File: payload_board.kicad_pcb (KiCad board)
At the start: 4 copper layers, 100 x 100 mm, 100 parts, among them IC1 RP2040_QFN56, IC2 AZ1117CH-3.3TRG1, J1 Cam_PicoLock, J10 503398-1892, J12 FC Breakout, J15 SWC, J2 Cam_Conn, J3 Antenna_Conn, J4 usb jumper, J5 Display_Conn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

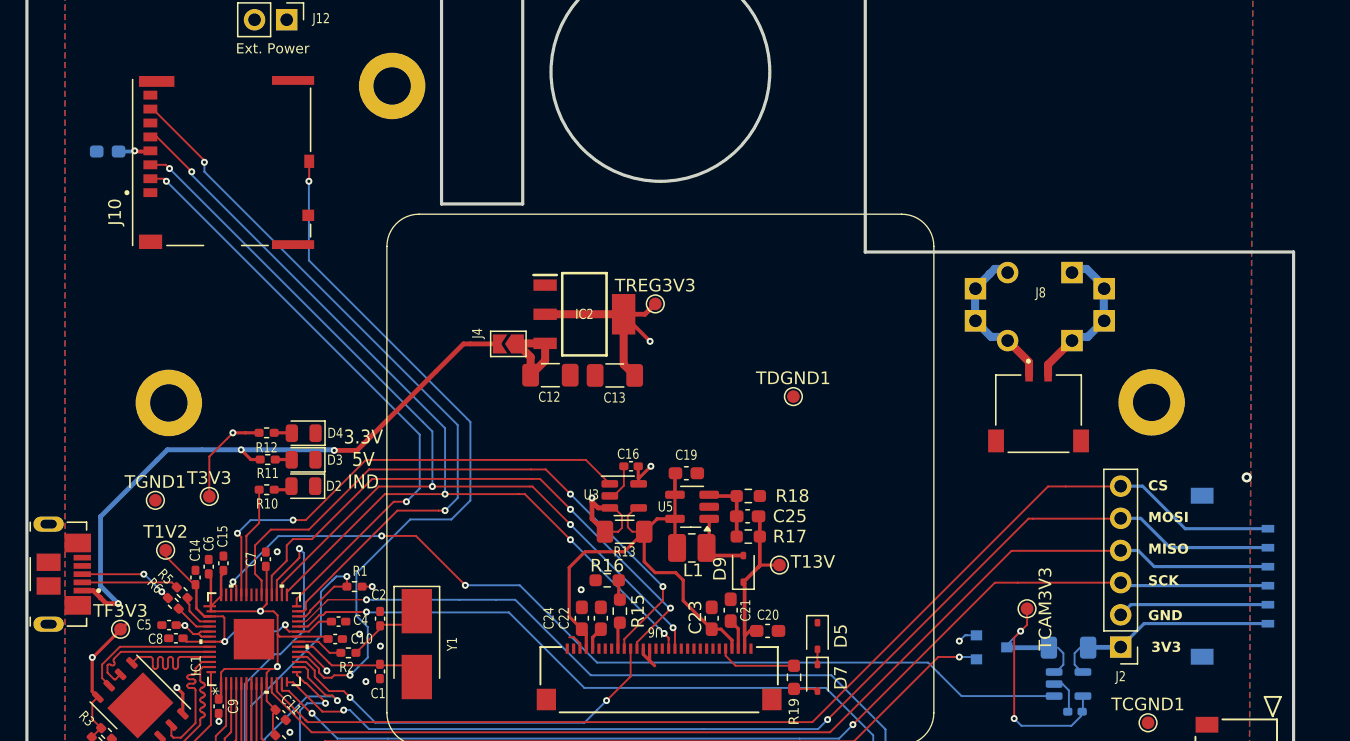
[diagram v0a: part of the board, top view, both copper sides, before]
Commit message: Moved the final connector from back to front, footprint kepout for chasis mounts and moved sd card
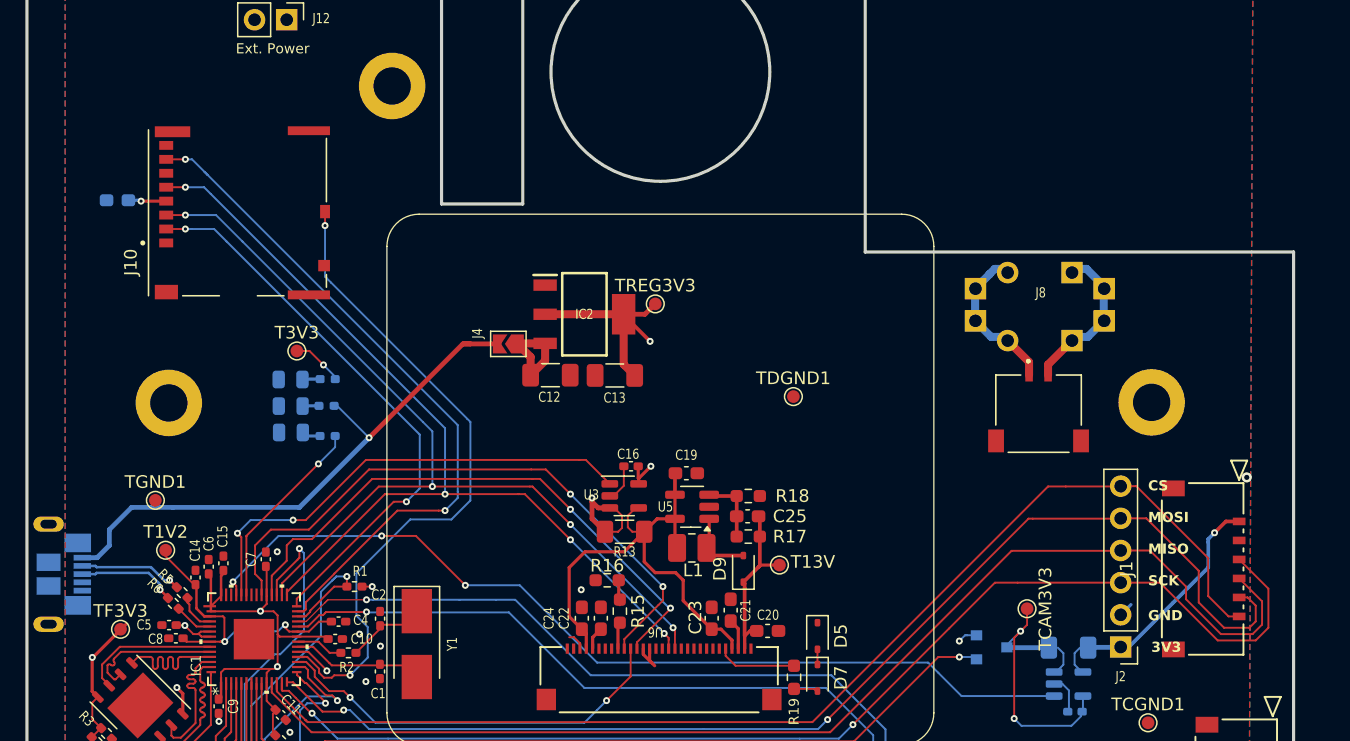
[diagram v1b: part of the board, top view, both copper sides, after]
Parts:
- D2, D3, D4, J7, R10, R11, R12: moved to B.Cu
- J1: moved to F.Cu
- moved T3V3 13.4 mm to (34.3, 58.9)
- moved J1 8.39 mm to (108.7, 72.4), turned to 90 degrees
- moved R12 6.42 mm to (36.7, 61.1), turned to 0 degrees
- moved R10 6.41 mm to (36.7, 65.6), turned to 0 degrees
- moved R11 6.29 mm to (36.6, 63.2), turned to 0 degrees
- moved D4 4.36 mm to (33.8, 61.1), turned to 0 degrees
- moved D3 4.36 mm to (33.8, 63.2), turned to 0 degrees
- moved D2 4.35 mm to (33.8, 65.3), turned to 0 degrees
- moved J10 4.16 mm to (29.6, 48.0)
- moved C18 3.92 mm to (20.1, 47.0)
- turned J7 to 90 degrees
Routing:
- net GND: track 27.9 -> 16.8 mm
- net SPI1_SCK_Cam: track 85.4 -> 94.1 mm
- net SPI1_MISO_Cam: track 87.4 -> 94.2 mm
- net Net-(IC1-GPIO25): track 8.81 -> 15.5 mm, vias 0 -> 1
- net SPI1_MOSI_Cam: track 87.1 -> 93.0 mm
- net VBUS: track 49.8 -> 45.0 mm, vias 3 -> 1
- net SD_IND: track 57.6 -> 53.1 mm
- net +3.3V: track 95.8 -> 92.3 mm
- net SPI0_MISO: track 57.6 -> 54.5 mm
- net SPI0_SCK: track 77.2 -> 74.2 mm
- net SPI0_CS_SD: track 47.8 -> 44.9 mm
- net SPI0_MOSI: track 77.1 -> 74.2 mm
- net SPI1_CS_Cam: track 89.2 -> 91.5 mm
- net CIN-: track 17.3 -> 19.4 mm, vias 0 -> 1
- net /D-: track 7.90 -> 8.16 mm, vias 0 -> 1
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
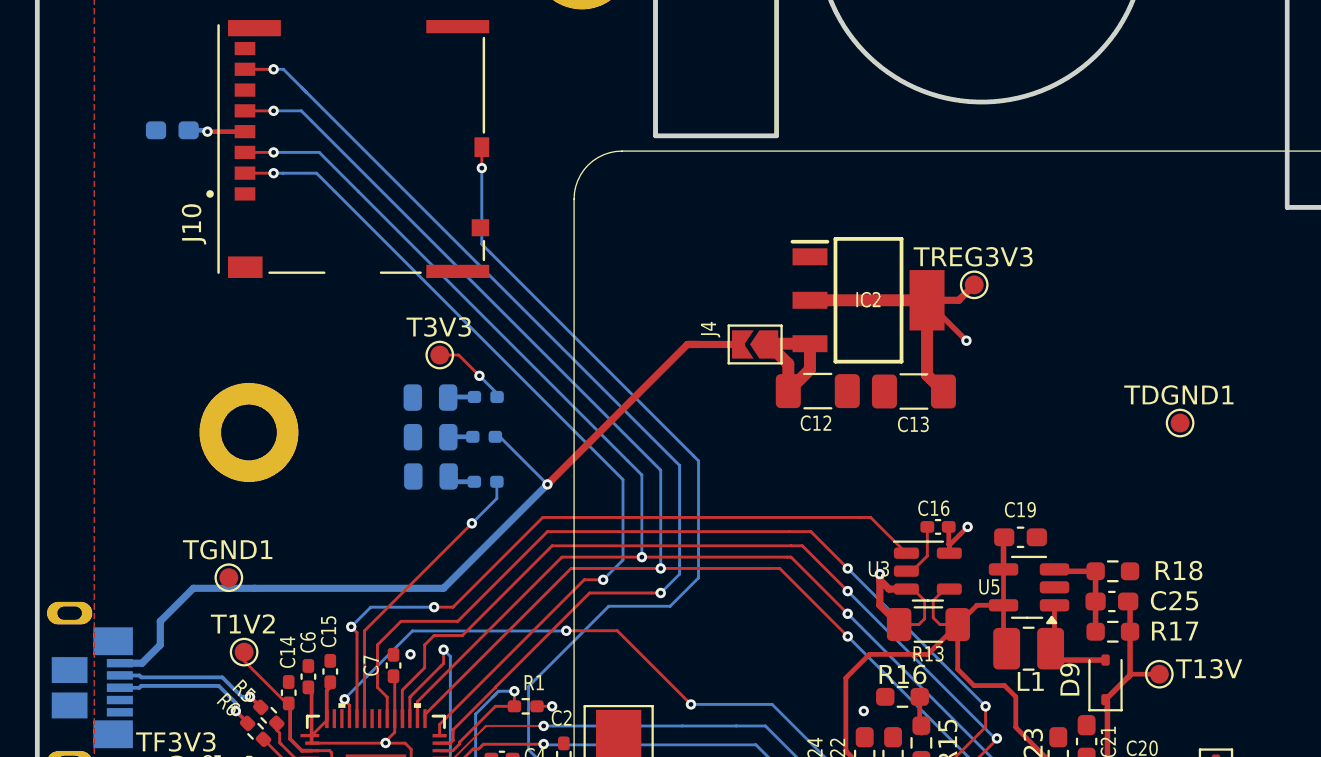
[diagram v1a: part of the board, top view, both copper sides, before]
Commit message: Changed some components to decrease bom count (C18, C25)
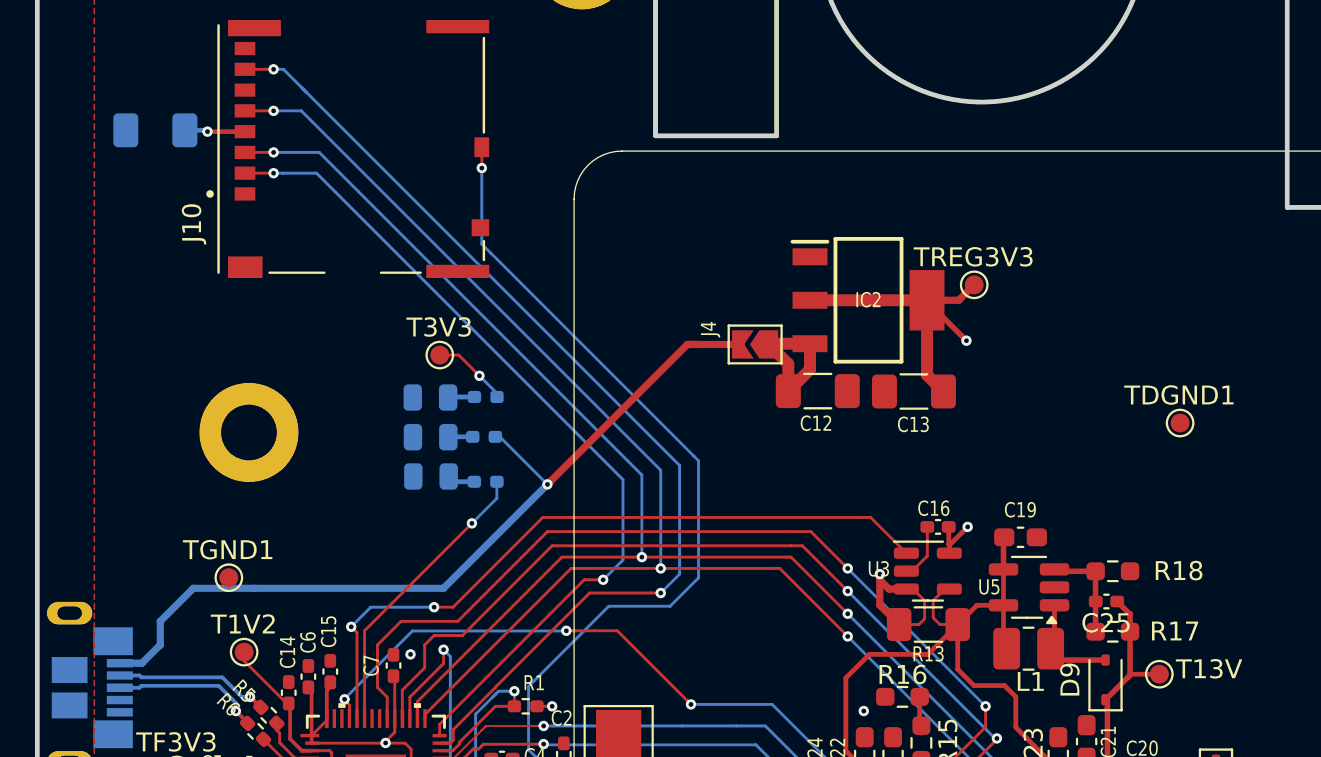
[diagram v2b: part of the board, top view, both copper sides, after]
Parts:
- C18: footprint Capacitor_SMD:C_0603_1608Metric_Pad1.08x0.95mm_HandSolder -> Capacitor_SMD:C_1206_3216Metric_Pad1.33x1.80mm_HandSolder
- C25: footprint Capacitor_SMD:C_0603_1608Metric_Pad1.08x0.95mm_HandSolder -> Capacitor_SMD:C_0402_1005Metric_Pad0.74x0.62mm_HandSolder
- moved C18 0.90 mm to (19.2, 47.0)
- moved C25 0.29 mm to (69.6, 72.0)
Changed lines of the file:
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@@
 		)
 	)
-	(footprint "Capacitor_SMD:C_0603_1608Metric_Pad1.08x0.95mm_HandSolder"
+	(footprint "Capacitor_SMD:C_0402_1005Metric_Pad0.74x0.62mm_HandSolder"
 		(layer "F.Cu")
-		(at 69.887499 71.95 180)
-		(descr "Capacitor SMD 0603 (1608 Metric), square (rectangular) end terminal, IPC_7351 nominal with elongated pad for handsoldering. (Body size source: IPC-SM-782 page 76, https://www.pcb-3d.com/wordpress/wp-content/uploads/ipc-sm-782a_amendment_1_and_2.pdf), generated with kicad-footprint-generator")
+		(at 69.6 71.95 180)
+		(descr "Capacitor SMD 0402 (1005 Metric), square (rectangular) end terminal, IPC_7351 nominal with elongated pad for handsoldering. (Body size source: IPC-SM-782 page 76, https://www.pcb-3d.com/wordpress/wp-content/uploads/ipc-sm-782a_amendment_1_and_2.pdf), generated with kicad-footprint-generator")
 		(tags "capacitor handsolder")
 		(property "Reference" "C25"
-			(at -3.3375 0 0)
+			(at 0 -1.16 180)
 			(layer "F.SilkS")
 			(effects
@@
 		)
 		(property "Value" "0.1uF"
-			(at 0 1.43 0)
+			(at 0 1.16 180)
 			(layer "F.Fab")
 			(effects
@@
 			)
 		)
-		(property "Footprint" "Capacitor_SMD:C_0603_1608Metric_Pad1.08x0.95mm_HandSolder"
+		(property "Footprint" "Capacitor_SMD:C_0402_1005Metric_Pad0.74x0.62mm_HandSolder"
 			(at 0 0 180)
 			(unlocked yes)
@@
 		(attr smd)
 		(fp_line
-			(start -0.146267 0.51)
-			(end 0.146267 0.51)
+			(start -0.115835 0.36)
+			(end 0.115835 0.36)
 			(stroke
 				(width 0.12)
@@
 		)
 		(fp_line
-			(start -0.146267 -0.51)
-			(end 0.146267 -0.51)
+			(start -0.115835 -0.36)
+			(end 0.115835 -0.36)
 			(stroke
 				(width 0.12)
@@
 		)
 		(fp_line
-			(start 1.65 0.73)
-			(end -1.65 0.73)
+			(start 1.08 0.46)
+			(end -1.08 0.46)
 			(stroke
 				(width 0.05)
@@
 		)
 		(fp_line
-			(start 1.65 -0.73)
-			(end 1.65 0.73)
+			(start 1.08 -0.46)
+			(end 1.08 0.46)
 			(stroke
 				(width 0.05)
@@
 		)
 		(fp_line
-			(start -1.65 0.73)
-			(end -1.65 -0.73)
+			(start -1.08 0.46)
+			(end -1.08 -0.46)
 			(stroke
 				(width 0.05)
@@
 		)
 		(fp_line
-			(start -1.65 -0.73)
-			(end 1.65 -0.73)
+			(start -1.08 -0.46)
+			(end 1.08 -0.46)
 			(stroke
 				(width 0.05)
@@
 		)
 		(fp_line
-			(start 0.8 0.4)
-			(end -0.8 0.4)
+			(start 0.5 0.25)
+			(end -0.5 0.25)
 			(stroke
 				(width 0.1)
@@
 		)
 		(fp_line
-			(start 0.8 -0.4)
-			(end 0.8 0.4)
+			(start 0.5 -0.25)
+			(end 0.5 0.25)
 			(stroke
 				(width 0.1)
@@
 		)
 		(fp_line
-			(start -0.8 0.4)
-			(end -0.8 -0.4)
+			(start -0.5 0.25)
+			(end -0.5 -0.25)
 			(stroke
 				(width 0.1)
@@
 		)
 		(fp_line
-			(start -0.8 -0.4)
-			(end 0.8 -0.4)
+			(start -0.5 -0.25)
+			(end 0.5 -0.25)
 			(stroke
 				(width 0.1)
@@
 		)
 		(fp_text user "${REFERENCE}"
-			(at 0 0 0)
+			(at 0 0 180)
 			(layer "F.Fab")
 			(effects
 				(font
-					(size 0.4 0.4)
-					(thickness 0.06)
+					(size 0.25 0.25)
+					(thickness 0.04)
 				)
 			)
 		)
 		(pad "1" smd roundrect
-			(at -0.8625 0 180)
-			(size 1.075 0.95)
+			(at -0.5675 0 180)
+			(size 0.735 0.62)
 			(layers "F.Cu" "F.Paste" "F.Mask")
 			(roundrect_rratio 0.25)
@@
 		)
 		(pad "2" smd roundrect
-			(at 0.8625 0 180)
-			(size 1.075 0.95)
+			(at 0.5675 0 180)
+			(size 0.735 0.62)
 			(layers "F.Cu" "F.Paste" "F.Mask")
 			(roundrect_rratio 0.25)
@@
 			(pintype "passive")
 		)
-		(model "${KICAD8_3DMODEL_DIR}/Capacitor_SMD.3dshapes/C_0603_1608Metric.wrl"
+		(model "${KICAD8_3DMODEL_DIR}/Capacitor_SMD.3dshapes/C_0402_1005Metric.wrl"
 			(offset
 				(xyz 0 0 0)
@@
 		)
 	)
-	(footprint "Capacitor_SMD:C_0603_1608Metric_Pad1.08x0.95mm_HandSolder"
+	(footprint "Capacitor_SMD:C_1206_3216Metric_Pad1.33x1.80mm_HandSolder"
 		(layer "B.Cu")
-		(at 20.1375 47)
-		(descr "Capacitor SMD 0603 (1608 Metric), square (rectangular) end terminal, IPC_7351 nominal with elongated pad for handsoldering. (Body size source: IPC-SM-782 page 76, https://www.pcb-3d.com/wordpress/wp-content/uploads/ipc-sm-782a_amendment_1_and_2.pdf), generated with kicad-footprint-generator")
+		(at 19.2375 47)
+		(descr "Capacitor SMD 1206 (3216 Metric), square (rectangular) end terminal, IPC_7351 nominal with elongated pad for handsoldering. (Body size source: IPC-SM-782 page 76, https://www.pcb-3d.com/wordpress/wp-content/uploads/ipc-sm-782a_amendment_1_and_2.pdf), generated with kicad-footprint-generator")
 		(tags "capacitor handsolder")
 		(property "Reference" "C18"
-			(at 0 1.43 0)
+			(at 0 1.85 180)
 			(layer "B.SilkS")
 			(effects
 				(font
-					(size 0.8 0.65)
+					(size 1 1)
 					(thickness 0.15)
 				)
@@
 		)
 		(property "Value" "10uF"
-			(at 0 -1.43 0)
+			(at 0 -1.85 180)
 			(layer "B.Fab")
 			(effects
 				(font
-					(size 0.8 0.65)
+					(size 1 1)
 					(thickness 0.15)
 				)
@@
 			)
 		)
-		(property "Footprint" "Capacitor_SMD:C_0603_1608Metric_Pad1.08x0.95mm_HandSolder"
+		(property "Footprint" "Capacitor_SMD:C_1206_3216Metric_Pad1.33x1.80mm_HandSolder"
 			(at 0 0 180)
 			(unlocked yes)
@@
 		(attr smd)
 		(fp_line
-			(start 0.146267 -0.51)
-			(end -0.146267 -0.51)
+			(start 0.711252 -0.91)
+			(end -0.711252 -0.91)
 			(stroke
 				(width 0.12)
@@
 		)
 		(fp_line
-			(start 0.146267 0.51)
-			(end -0.146267 0.51)
+			(start 0.711252 0.91)
+			(end -0.711252 0.91)
 			(stroke
 				(width 0.12)
@@
 		)
 		(fp_line
-			(start -1.65 -0.73)
-			(end 1.65 -0.73)
+			(start -2.48 -1.15)
+			(end 2.48 -1.15)
 			(stroke
 				(width 0.05)
@@
 		)
 		(fp_line
-			(start -1.65 0.73)
-			(end -1.65 -0.73)
+			(start -2.48 1.15)
+			(end -2.48 -1.15)
 			(stroke
 				(width 0.05)
@@
 		)
 		(fp_line
-			(start 1.65 -0.73)
-			(end 1.65 0.73)
+			(start 2.48 -1.15)
+			(end 2.48 1.15)
 			(stroke
 				(width 0.05)
@@
 		)
 		(fp_line
-			(start 1.65 0.73)
-			(end -1.65 0.73)
+			(start 2.48 1.15)
+			(end -2.48 1.15)
 			(stroke
 				(width 0.05)
@@
 		)
 		(fp_line
-			(start -0.8 -0.4)
-			(end 0.8 -0.4)
+			(start -1.6 -0.8)
+			(end 1.6 -0.8)
 			(stroke
 				(width 0.1)
@@
 		)
 		(fp_line
-			(start -0.8 0.4)
-			(end -0.8 -0.4)
+			(start -1.6 0.8)
+			(end -1.6 -0.8)
 			(stroke
 				(width 0.1)
@@
 		)
 		(fp_line
-			(start 0.8 -0.4)
-			(end 0.8 0.4)
+			(start 1.6 -0.8)
+			(end 1.6 0.8)
 			(stroke
 				(width 0.1)
@@
 		)
 		(fp_line
-			(start 0.8 0.4)
-			(end -0.8 0.4)
+			(start 1.6 0.8)
+			(end -1.6 0.8)
 			(stroke
 				(width 0.1)
@@
 		)
 		(fp_text user "${REFERENCE}"
-			(at 0 0 0)
+			(at 0 0 180)
 			(layer "B.Fab")
 			(effects
 				(font
-					(size 0.8 0.65)
-					(thickness 0.15)
+					(size 0.8 0.8)
+					(thickness 0.12)
 				)
 				(justify mirror)
@@
 		)
 		(pad "1" smd roundrect
-			(at -0.8625 0)
-			(size 1.075 0.95)
+			(at -1.5625 0)
+			(size 1.325 1.8)
 			(layers "B.Cu" "B.Paste" "B.Mask")
-			(roundrect_rratio 0.25)
+			(roundrect_rratio 0.188679)
 			(net 1 "GND")
 			(pintype "passive")
 		)
 		(pad "2" smd roundrect
-			(at 0.8625 0)
-			(size 1.075 0.95)
+			(at 1.5625 0)
+			(size 1.325 1.8)
 			(layers "B.Cu" "B.Paste" "B.Mask")
-			(roundrect_rratio 0.25)
+			(roundrect_rratio 0.188679)
 			(net 43 "+3.3V")
 			(pintype "passive")
 		)
-		(model "${KICAD8_3DMODEL_DIR}/Capacitor_SMD.3dshapes/C_0603_1608Metric.wrl"
+		(model "${KICAD8_3DMODEL_DIR}/Capacitor_SMD.3dshapes/C_1206_3216Metric.wrl"
 			(offset
 				(xyz 0 0 0)
@@
 		)
 		(property "Footprint" ""
-			(at 0 0 360)
+			(at 0 0 0)
 			(layer "B.Fab")
 			(hide yes)
@@
 		)
 		(property "Datasheet" ""
-			(at 0 0 360)
+			(at 0 0 0)
 			(layer "B.Fab")
 			(hide yes)
@@
 		)
 		(property "Description" "Light emitting diode"
-			(at 0 0 360)
+			(at 0 0 0)
 			(layer "B.Fab")
 			(hide yes)
@@
 		)
 		(property "Footprint" ""
-			(at 0 0 360)
+			(at 0 0 0)
 			(layer "B.Fab")
 			(hide yes)
@@
 		)
 		(property "Datasheet" ""
-			(at 0 0 360)
+			(at 0 0 0)
 			(layer "B.Fab")
 			(hide yes)
@@
 		)
 		(property "Description" "Light emitting diode"
-			(at 0 0 360)
+			(at 0 0 0)
 			(layer "B.Fab")
 			(hide yes)
@@
 	)
 	(segment
-		(start 70.849999 73.55)
-		(end 70.849999 72.05)
+		(start 70.8175 72.6)
+		(end 70.1675 71.95)
 		(width 0.29337)
 		(layer "F.Cu")
@@
 	)
 	(segment
-		(start 69.649999 81.4)
-		(end 69.649999 77.6)
+		(start 70.849999 73.55)
+		(end 70.849999 72.6)
 		(width 0.29337)
 		(layer "F.Cu")
@@
 	)
 	(segment
-		(start 70.749999 75.949999)
-		(end 70.849999 75.85)
+		(start 69.649999 81.4)
+		(end 69.649999 77.6)
 		(width 0.29337)
 		(layer "F.Cu")
@@
 	)
 	(segment
-		(start 70.849999 72.05)
-		(end 70.749999 71.95)
+		(start 70.749999 75.949999)
+		(end 70.849999 75.85)
 		(width 0.29337)
 		(layer "F.Cu")
@@
 		(layer "F.Cu")
 		(net 64)
+	)
+	(segment
+		(start 70.849999 72.6)
+		(end 70.8175 72.6)
+		(width 0.29337)
+		(layer "F.Cu")
+		(net 64)
